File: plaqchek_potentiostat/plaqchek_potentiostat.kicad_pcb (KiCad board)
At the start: 2 copper layers, 46 x 59.8 mm, 57 parts, among them J1 Conn_01x03, J2 Conn_01x03, J3 Conn_01x02, SW2 SW_SPDT, U1 TL082, U3 TL082, U4 TL082, U5 TPS7A2050PDBVR, U6 MC79M05_TO252

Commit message: more routing
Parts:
- moved TP13 14.7 mm to (171.0, 143.8)
- moved TP8 7.11 mm to (174.8, 131.8)
- moved TP11 3.43 mm to (179.0, 122.0)
- moved TP1 2.14 mm to (179.0, 115.0)
- moved R9 1.88 mm to (171.5, 140.3), turned to -90 degrees
- moved TP10 1.52 mm to (177.4, 98.4)
- moved C7 0.78 mm to (168.6, 132.7)
- moved R1 0.78 mm to (162.0, 136.0)
- moved C8 0.70 mm to (166.8, 138.9)
- moved R4 0.70 mm to (162.0, 133.1)
- moved RV3 0.70 mm to (157.2, 141.4)
- moved U4 0.70 mm to (167.7, 135.6)
- moved TP7 0.70 mm to (167.2, 142.2)
- moved R11 0.37 mm to (172.7, 135.4)
- moved C12 0.28 mm to (180.6, 96.0)
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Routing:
- net -6V5: track 0.00 -> 28.2 mm, vias 0 -> 2
- net /VBIAS_POT_P: track 0.00 -> 23.3 mm, vias 0 -> 2
- net GND: track 0.00 -> 18.8 mm, vias 0 -> 8
- net Net-(U4A-+): track 0.00 -> 16.9 mm
- net +6V: track 0.00 -> 15.2 mm
- net /VBIAS_POT_N: track 0.00 -> 9.38 mm
- net +5VA: track 4.30 -> 12.1 mm, vias 0 -> 7
- net Net-(U4B--): track 0.00 -> 6.73 mm
- net Net-(U5-OUT): track 0.00 -> 5.63 mm
- net -5VA: track 4.40 -> 8.16 mm, vias 0 -> 1
- net /REF_ELEC: track 12.7 -> 16.3 mm
- net /WORKING_ELEC: track 12.3 -> 15.6 mm
- net Net-(U5-EN): track 0.00 -> 2.20 mm
- added copper zone on F.Cu, net +5VA
- added copper zone on In2.Cu, net +5VA
- added copper zone on F.Cu, net +6V
- added copper zone on In2.Cu, net -5VA
- added copper zone on F.Cu, net -6V5
- added copper zone on B.Cu, net GND
- added copper zone on F.Cu, net GND
- added copper zone on In1.Cu, net GND
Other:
- board size 46 x 59.8 mm -> 46 x 59 mm
- copper layers 2 -> 4

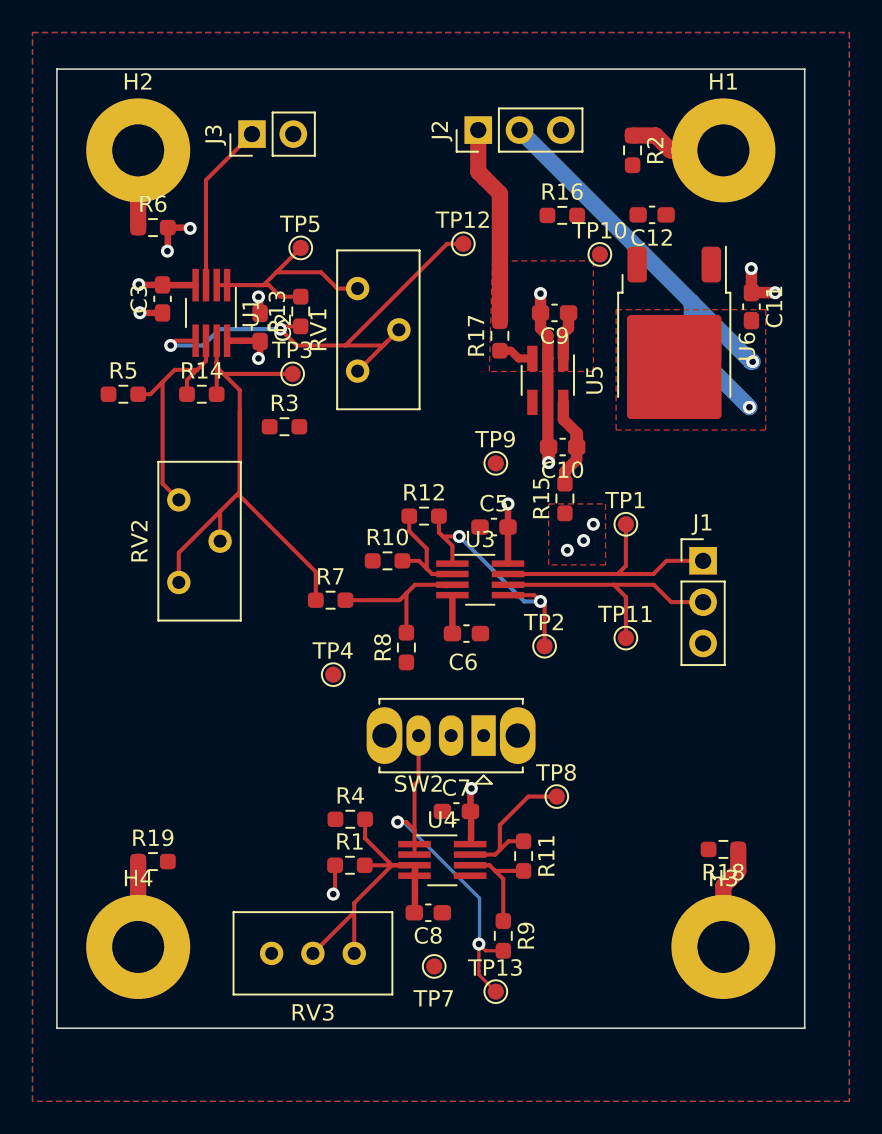
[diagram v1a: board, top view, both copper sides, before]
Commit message: finish potentiostat board, update board constraints
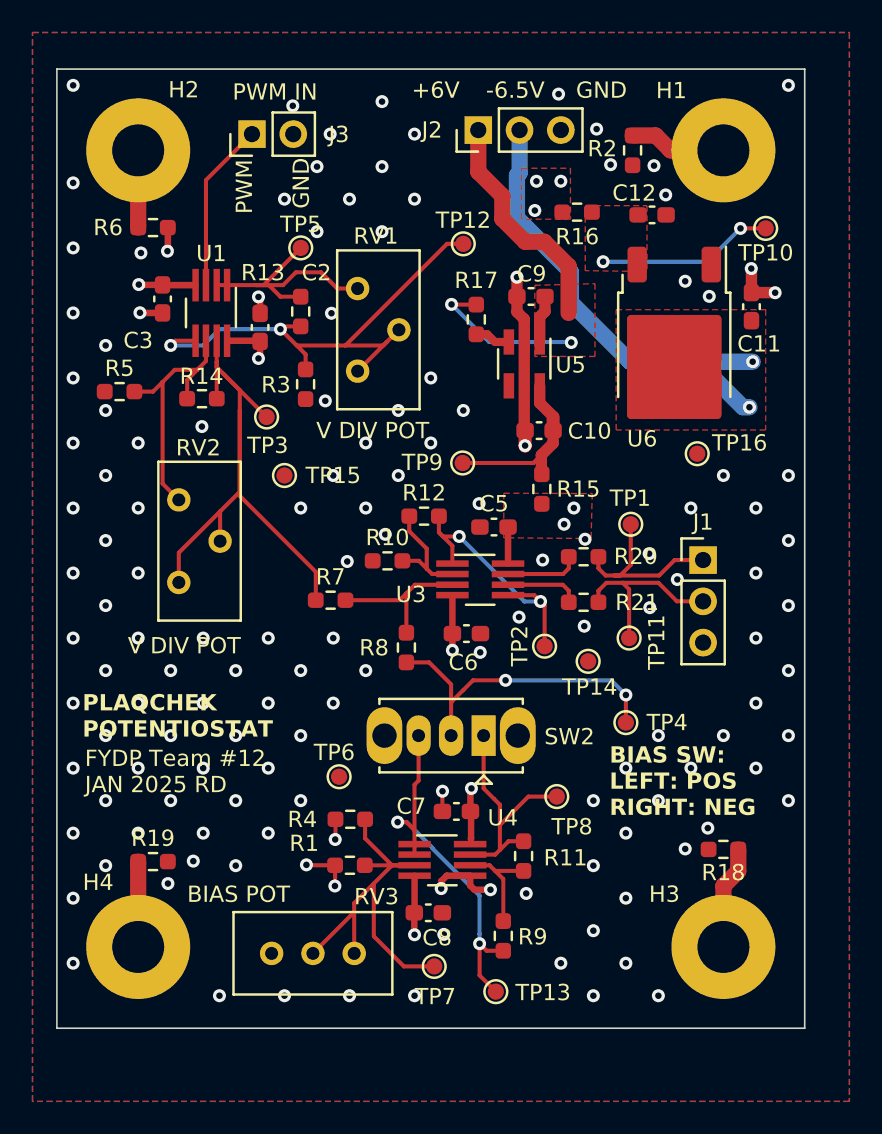
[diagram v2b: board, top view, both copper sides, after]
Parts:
- added R20: 0R, Resistor_SMD:R_0603_1608Metric_Pad0.98x0.95mm_HandSolder, F.Cu at (176.4, 117.0)
- added R21: 0R, Resistor_SMD:R_0603_1608Metric_Pad0.98x0.95mm_HandSolder, F.Cu at (176.4, 119.8)
- added TP14: TestPoint, TestPoint:TestPoint_Pad_D1.0mm, F.Cu at (176.7, 123.4)
- added TP15: TestPoint, TestPoint:TestPoint_Pad_D1.0mm, F.Cu at (158.0, 112.0)
- added TP16: TestPoint, TestPoint:TestPoint_Pad_D1.0mm, F.Cu at (183.4, 110.7)
- added TP6: TestPoint, TestPoint:TestPoint_Pad_D1.0mm, F.Cu at (161.4, 130.5)
- moved TP4 18.2 mm to (179.0, 127.2)
- moved TP10 10.3 mm to (187.6, 96.8)
- moved TP3 3.10 mm to (156.9, 108.4)
- moved R3 2.92 mm to (159.3, 106.4), turned to 90 degrees
- moved TP9 2.04 mm to (169.0, 111.2)
- moved C10 1.77 mm to (173.7, 109.2)
- moved C9 1.77 mm to (173.2, 101.0)
- moved U5 1.77 mm to (172.8, 105.1)
- moved R17 1.77 mm to (169.8, 102.4)
- moved R15 1.53 mm to (173.8, 112.8)
- moved R16 0.93 mm to (176.0, 95.8)
- moved TP1 0.30 mm to (179.3, 115.0)
- moved R5 0.28 mm to (147.9, 106.8)
- moved R14 0.28 mm to (152.9, 107.3)
- moved TP11 0.20 mm to (179.2, 122.0)
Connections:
- net Net-(U5-OUT) renamed /5V_R
- net Net-(U6-VO) renamed /-5V_R
- U3 pad 6: /REF_ELEC -> Net-(U3B--)
- U3 pad 7: /WORKING_ELEC -> Net-(R20-Pad2)
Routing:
- net /VBIAS_POT: track 0.00 -> 19.9 mm, vias 0 -> 2
- net +6V: track 15.2 -> 27.0 mm, vias 0 -> 2
- net /-5V_R: track 0.00 -> 10.8 mm, vias 0 -> 2
- net Net-(U4A-+): track 16.9 -> 24.7 mm
- net /VBIAS_POT_N: track 9.38 -> 15.4 mm
- net /5V_R: track 5.63 -> 11.1 mm
- net GND: track 18.8 -> 24.3 mm, vias 8 -> 142
- net /REF_ELEC: track 16.3 -> 11.4 mm
- net Net-(U3B--): track 0.00 -> 4.60 mm
- net Net-(R20-Pad2): track 0.00 -> 4.59 mm
- net /WORKING_ELEC: track 15.6 -> 11.5 mm
- net -5VA: track 8.16 -> 10.5 mm, vias 1 -> 6
- net Net-(U1B-+): track 30.6 -> 32.3 mm
- net Net-(U1A--): track 14.6 -> 15.6 mm
- net -6V5: track 28.2 -> 29.1 mm
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- added copper zone on F.Cu, net -5VA
- added copper zone on F.Cu, net /-5V_R
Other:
- board text added: "+6V"
- board text added: "-6.5V"
- board text added: "BIAS POT"
- board text added: "BIAS SW: LEFT: POS RIGHT: NEG"
- board text added: "FYDP Team #12 JAN 2025 RD"
- board text added: "GND"
- board text added: "PLAQCHEK POTENTIOSTAT"
- board text added: "PWM"
- board text added: "PWM IN"
- board text added: "V DIV POT"

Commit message: finish all pcbs, generate gerber files
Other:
- board text added: "AMP POT"
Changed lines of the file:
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@@
       (outputformat 1)
       (mirror false)
-      (drillshape 1)
+      (drillshape 0)
       (scaleselection 1)
-      (outputdirectory "")
+      (outputdirectory "plaqchek_potentiostat_gerbers/")
     )
   )
@@
     (fp_line (start 4.11 2.7) (end 3.11 2.7)
       (stroke (width 0.1) (type solid)) (layer "F.Fab"))
-    (pad "1" smd roundrect (at -5.04 -2.28 270) (size 2.2 1.2) (layers "F.Cu" "F.Paste" "F.Mask") (roundrect_rratio 0.208333)
+    (pad "1" smd roundrect (at -5.04 -2.28 270) (size 2.2 1.2) (layers "F.Cu" "F.Paste" "F.Mask") (roundrect_rratio 0.2083333333)
       (net 1 "GND") (pinfunction "GND") (pintype "power_in"))
-    (pad "2" smd roundrect (at -0.415 -1.525 270) (size 3.05 2.75) (layers "F.Cu" "F.Paste") (roundrect_rratio 0.090909)
+    (pad "2" smd roundrect (at -0.415 -1.525 270) (size 3.05 2.75) (layers "F.Cu" "F.Paste") (roundrect_rratio 0.09090909091)
       (net 6 "-6V5") (pinfunction "VI") (pintype "power_in"))
-    (pad "2" smd roundrect (at -0.415 1.525 270) (size 3.05 2.75) (layers "F.Cu" "F.Paste") (roundrect_rratio 0.090909)
+    (pad "2" smd roundrect (at -0.415 1.525 270) (size 3.05 2.75) (layers "F.Cu" "F.Paste") (roundrect_rratio 0.09090909091)
       (net 6 "-6V5") (pinfunction "VI") (pintype "power_in"))
-    (pad "2" smd roundrect (at 1.26 0 270) (size 6.4 5.8) (layers "F.Cu" "F.Mask") (roundrect_rratio 0.043103)
+    (pad "2" smd roundrect (at 1.26 0 270) (size 6.4 5.8) (layers "F.Cu" "F.Mask") (roundrect_rratio 0.04310293103)
       (net 6 "-6V5") (pinfunction "VI") (pintype "power_in"))
-    (pad "2" smd roundrect (at 2.935 -1.525 270) (size 3.05 2.75) (layers "F.Cu" "F.Paste") (roundrect_rratio 0.090909)
+    (pad "2" smd roundrect (at 2.935 -1.525 270) (size 3.05 2.75) (layers "F.Cu" "F.Paste") (roundrect_rratio 0.09090909091)
       (net 6 "-6V5") (pinfunction "VI") (pintype "power_in"))
-    (pad "2" smd roundrect (at 2.935 1.525 270) (size 3.05 2.75) (layers "F.Cu" "F.Paste") (roundrect_rratio 0.090909)
+    (pad "2" smd roundrect (at 2.935 1.525 270) (size 3.05 2.75) (layers "F.Cu" "F.Paste") (roundrect_rratio 0.09090909091)
       (net 6 "-6V5") (pinfunction "VI") (pintype "power_in"))
-    (pad "3" smd roundrect (at -5.04 2.28 270) (size 2.2 1.2) (layers "F.Cu" "F.Paste" "F.Mask") (roundrect_rratio 0.208333)
+    (pad "3" smd roundrect (at -5.04 2.28 270) (size 2.2 1.2) (layers "F.Cu" "F.Paste" "F.Mask") (roundrect_rratio 0.2083333333)
       (net 7 "/-5V_R") (pinfunction "VO") (pintype "power_out"))
     (model "${KICAD6_3DMODEL_DIR}/Package_TO_SOT_SMD.3dshapes/TO-252-2.wrl"
@@
     (effects (font (size 1 1) (thickness 0.153) bold) (justify left bottom))
   )
-  (gr_text "V DIV POT" (at 148.36 123.06) (layer "F.SilkS" knockout)
+  (gr_text "AMP POT" (at 149.55 122.79) (layer "F.SilkS" knockout)
     (effects (font (size 1 1) (thickness 0.153)) (justify left bottom))
   )
@@
   )
   (gr_text "PLAQCHEK\nPOTENTIOSTAT" (at 145.57 128.18) (layer "F.SilkS")
-    (effects (font (size 1 1) (thickness 0.153) bold) (justify left bottom))
+    (effects (font (size 1.5 1.5) (thickness 0.3) bold) (justify left bottom))
   )
   (gr_text "-6.5V\n" (at 172.2 88.3) (layer "F.SilkS" knockout)
